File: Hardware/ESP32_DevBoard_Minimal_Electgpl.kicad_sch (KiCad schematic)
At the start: 36 parts, among them J1 U254-051T-4BH83-F1S, J2 Conn_01x22_Pin, J3 Conn_01x22_Pin, SW1 SW_Push, U1 MCP1826S-3302E/DB, U2 ESP32-S3, U3 W25Q64JVSSIQ, Y1 R940000096

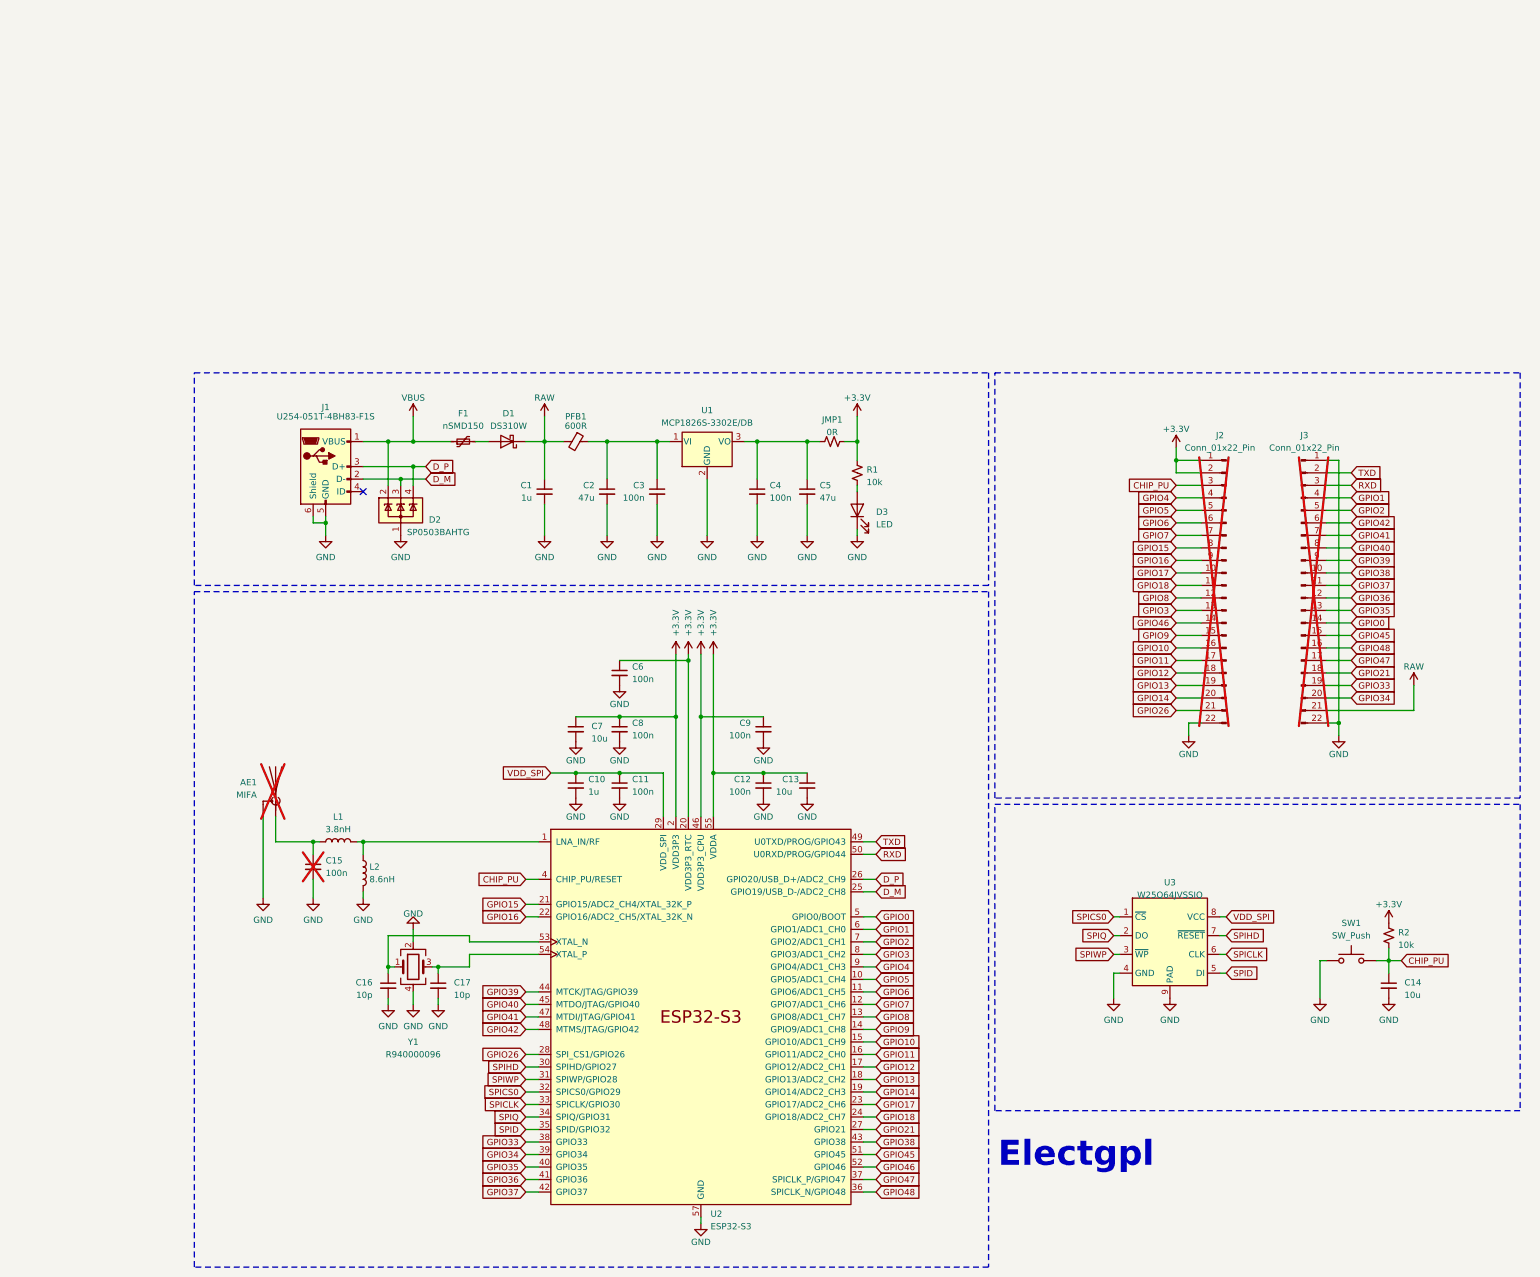
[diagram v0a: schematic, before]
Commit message: feather format and DRC check
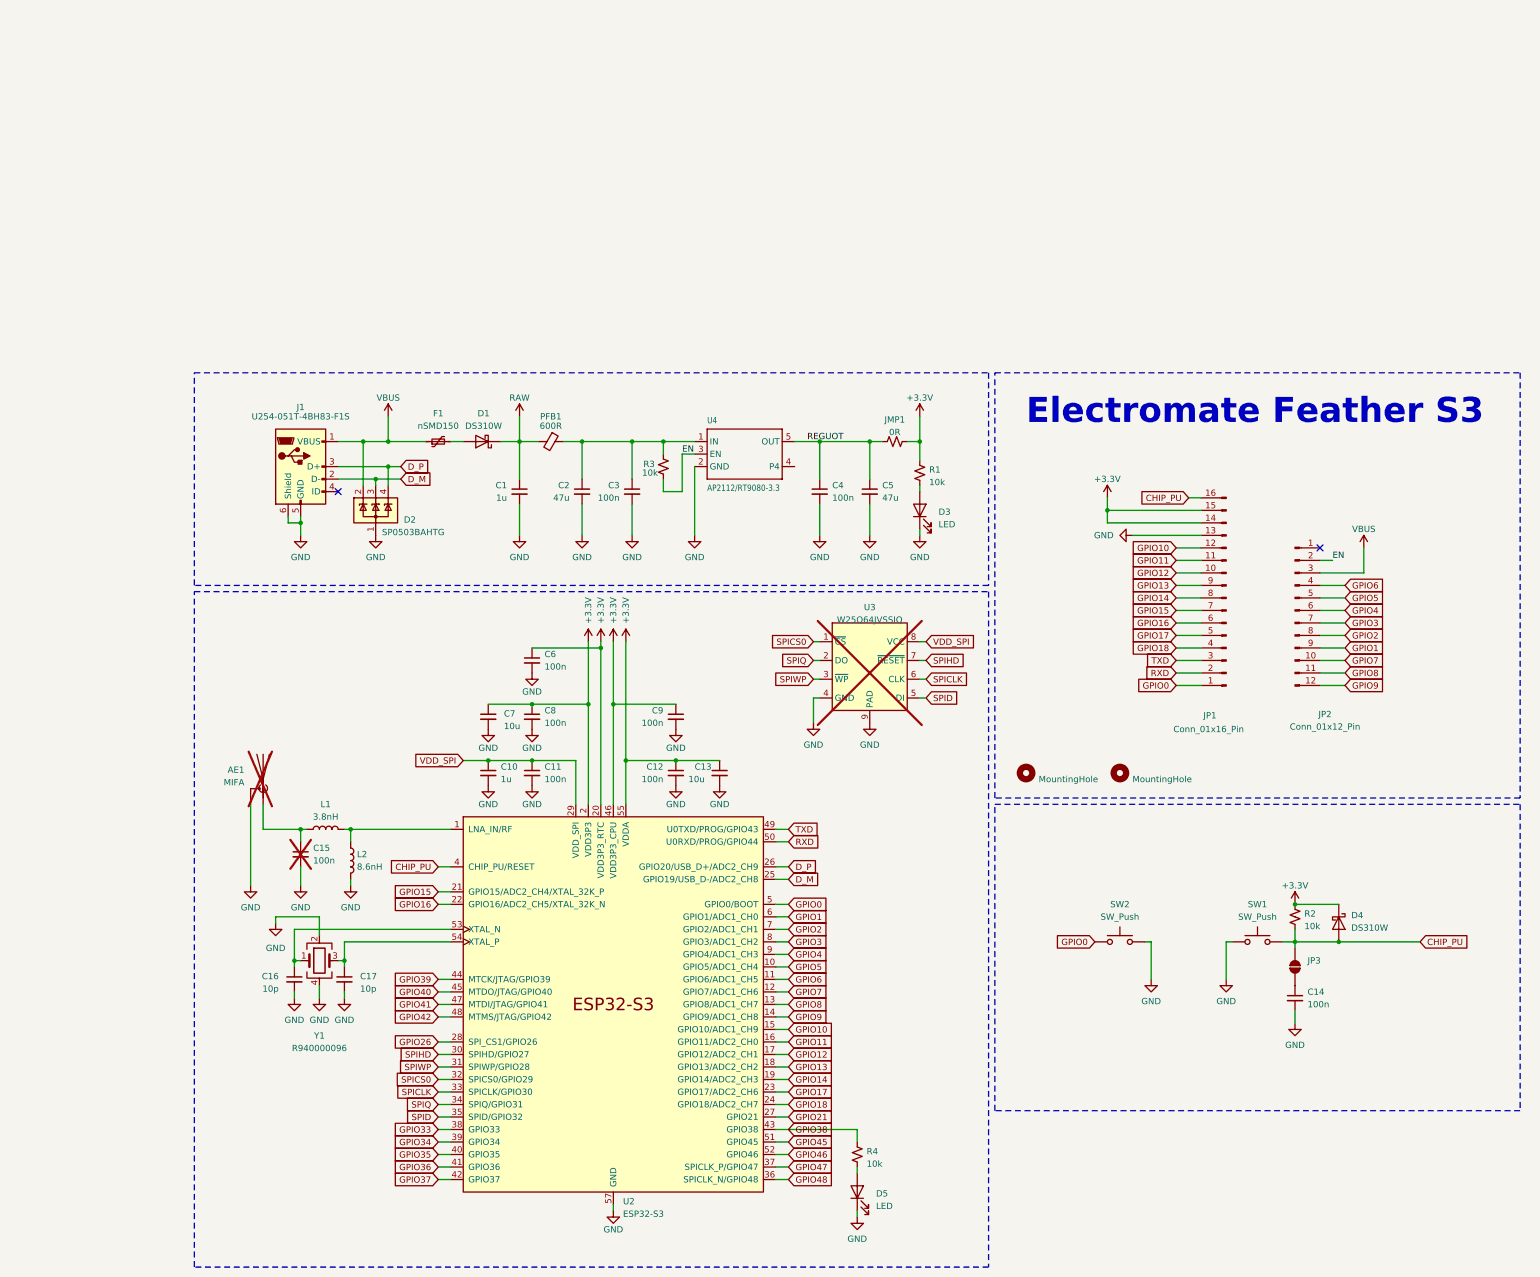
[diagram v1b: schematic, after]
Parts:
- removed U1: MCP1826S-3302E/DB, Package_TO_SOT_SMD:SOT-223, symbol Regulator_Linear:MCP1703Ax-330xxDB
- added D4: DS310W, Diode_SMD:D_SOD-123, symbol Diode:B140-E3
- added D5: LED, LED_SMD:LED_0603_1608Metric, symbol Device:LED
- added H1, H2: MountingHole, symbol Mechanical:MountingHole
- added JP3: SolderJumper_2_Open, Jumper:SolderJumper-2_P1.3mm_Open_RoundedPad1.0x1.5mm, symbol Jumper:SolderJumper_2_Open
- added R3, R4: 10k, Resistor_SMD:R_0402_1005Metric, symbol Device:R_Small_US
- added SW2: SW_Push, Button_Switch_SMD:SW_Push_SPST_NO_Alps_SKRK, symbol Switch:SW_Push
- added U4: AP2112/RT9080-3.3, Package_TO_SOT_SMD:SOT-23-5_HandSoldering, symbol Adafruit ESP32-S3 8MB No PSRAM-eagle-import:VREG_SOT23-5
- C1: LCSC Part Number (none) -> C5673; MFR P/N CL05X105KP5NNNC -> (none); MPN (none) -> CL05X105KP5NNNC; Reference MFG P/N C5673 -> (none)
- C14: value 10u -> 100n; footprint Capacitor_SMD:C_0603_1608Metric -> Capacitor_SMD:C_0402_1005Metric; Absolute minimum (none) -> 50V; LCSC CA0384128 -> RE0187778; MFR P/N GCM188D70J106ME36D -> CC0402KRX7R9BB104; Reference MFG P/N (none) -> C1591
- C2: LCSC Part Number (none) -> C124129; Reference MFG P/N C124129 -> (none)
- C3: LCSC Part Number (none) -> C1591; MFR P/N CC0402KRX7R9BB104 -> (none); MPN (none) -> CC0402KRX7R9BB104; Reference MFG P/N C1591 -> (none)
- JP1: renamed from J3; value Conn_01x22_Pin -> Conn_01x16_Pin; footprint Connector_PinHeader_2.54mm:PinHeader_1x22_P2.54mm_Vertical -> Connector_PinHeader_2.54mm:PinHeader_1x16_P2.54mm_Vertical; symbol Connector:Conn_01x22_Pin -> Connector:Conn_01x16_Pin; now fitted
- JP2: renamed from J2; value Conn_01x22_Pin -> Conn_01x12_Pin; footprint Connector_PinHeader_2.54mm:PinHeader_1x22_P2.54mm_Vertical -> Connector_PinHeader_2.54mm:PinHeader_1x12_P2.54mm_Vertical; symbol Connector:Conn_01x22_Pin -> Connector:Conn_01x12_Pin; now fitted
- U2: LCSC RF15788811 -> (none); LCSC Part Number (none) -> C3013940; MFR P/N ESP32-S3R8 -> (none); MPN (none) -> ESP32-S3FH4R2
- U3: now not fitted
- Y1: LCSC C7206306 -> (none); LCSC Part Number (none) -> C7206306
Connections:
- net +3.3V: now also JP1.14 (Pin_14), JP1.15 (Pin_15), D4.1 (K); no longer JP2.1 (Pin_1), JP2.2 (Pin_2)
- net CHIP_PU: now also JP1.16 (Pin_16), D4.2 (A), JP3.2 (B); no longer C14.1, JP2.3 (Pin_3)
- net GND: now also JP1.13 (Pin_13), D5.1 (K), SW2.1, U4.2 (GND); no longer JP1.1 (Pin_1), JP1.22 (Pin_22), JP2.22 (Pin_22)
- net GPIO0: now also JP1.1 (Pin_1), SW2.2; no longer JP1.14 (Pin_14)
- net GPIO1: now also JP2.9 (Pin_9); no longer JP1.4 (Pin_4)
- net GPIO10: now also JP1.12 (Pin_12); no longer JP2.16 (Pin_16)
- net GPIO11: now also JP1.11 (Pin_11); no longer JP2.17 (Pin_17)
- net GPIO12: now also JP1.10 (Pin_10); no longer JP2.18 (Pin_18)
- net GPIO13: now also JP1.9 (Pin_9); no longer JP2.19 (Pin_19)
- net GPIO14: now also JP1.8 (Pin_8); no longer JP2.20 (Pin_20)
- net GPIO15: now also JP1.7 (Pin_7); no longer JP2.8 (Pin_8)
- net GPIO16: now also JP1.6 (Pin_6); no longer JP2.9 (Pin_9)
- net GPIO17: now also JP1.5 (Pin_5); no longer JP2.10 (Pin_10)
- net GPIO18: now also JP1.4 (Pin_4); no longer JP2.11 (Pin_11)
- net GPIO2: now also JP2.8 (Pin_8); no longer JP1.5 (Pin_5)
- net GPIO21: no longer JP1.18 (Pin_18)
- net GPIO26: no longer JP2.21 (Pin_21)
- net GPIO3: now also JP2.7 (Pin_7); no longer JP2.13 (Pin_13)
- net GPIO33: no longer JP1.19 (Pin_19)
- net GPIO34: no longer JP1.20 (Pin_20)
- net GPIO35: no longer JP1.13 (Pin_13)
- net GPIO36: no longer JP1.12 (Pin_12)
- net GPIO37: no longer JP1.11 (Pin_11)
- net GPIO38: now also R4.1; no longer JP1.10 (Pin_10)
- net GPIO39: no longer JP1.9 (Pin_9)
- net GPIO4: now also JP2.6 (Pin_6); no longer JP2.4 (Pin_4)
- net GPIO40: no longer JP1.8 (Pin_8)
- net GPIO41: no longer JP1.7 (Pin_7)
- net GPIO42: no longer JP1.6 (Pin_6)
- net GPIO45: no longer JP1.15 (Pin_15)
- net GPIO46: no longer JP2.14 (Pin_14)
- net GPIO47: no longer JP1.17 (Pin_17)
- net GPIO48: no longer JP1.16 (Pin_16)
- net GPIO6: now also JP2.4 (Pin_4); no longer JP2.6 (Pin_6)
- net GPIO7: now also JP2.10 (Pin_10); no longer JP2.7 (Pin_7)
- net GPIO8: now also JP2.11 (Pin_11); no longer JP2.12 (Pin_12)
- net GPIO9: now also JP2.12 (Pin_12); no longer JP2.15 (Pin_15)
- net RAW: no longer JP1.21 (Pin_21)
- net RXD: now also JP1.2 (Pin_2); no longer JP1.3 (Pin_3)
- net TXD: now also JP1.3 (Pin_3); no longer JP1.2 (Pin_2)
- net VBUS: now also JP2.3 (Pin_3)
- net REGUOT: now reaches C4.1, C5.1, JMP1.1
- net REGUOT: now also U4.5 (OUT)
- net at C2.1, C3.1, PFB1.1: now also R3.1, U4.1 (IN)
- new net: D5.2 (A), R4.2
- new net: C14.1, JP3.1 (A)
- new net EN: JP2.2 (Pin_2), R3.2, U4.3 (EN)
- no-connect marks 1 -> 2
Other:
- note added: "Electromate Feather S3"
- note removed: "Electgpl"
- company: Electgpl -> Electromate
- moved on the sheet: AE1, C1, C10, C11, C12, C13, C15, C16, C17, C2, C3, C4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

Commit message: add u.FL antenna connector
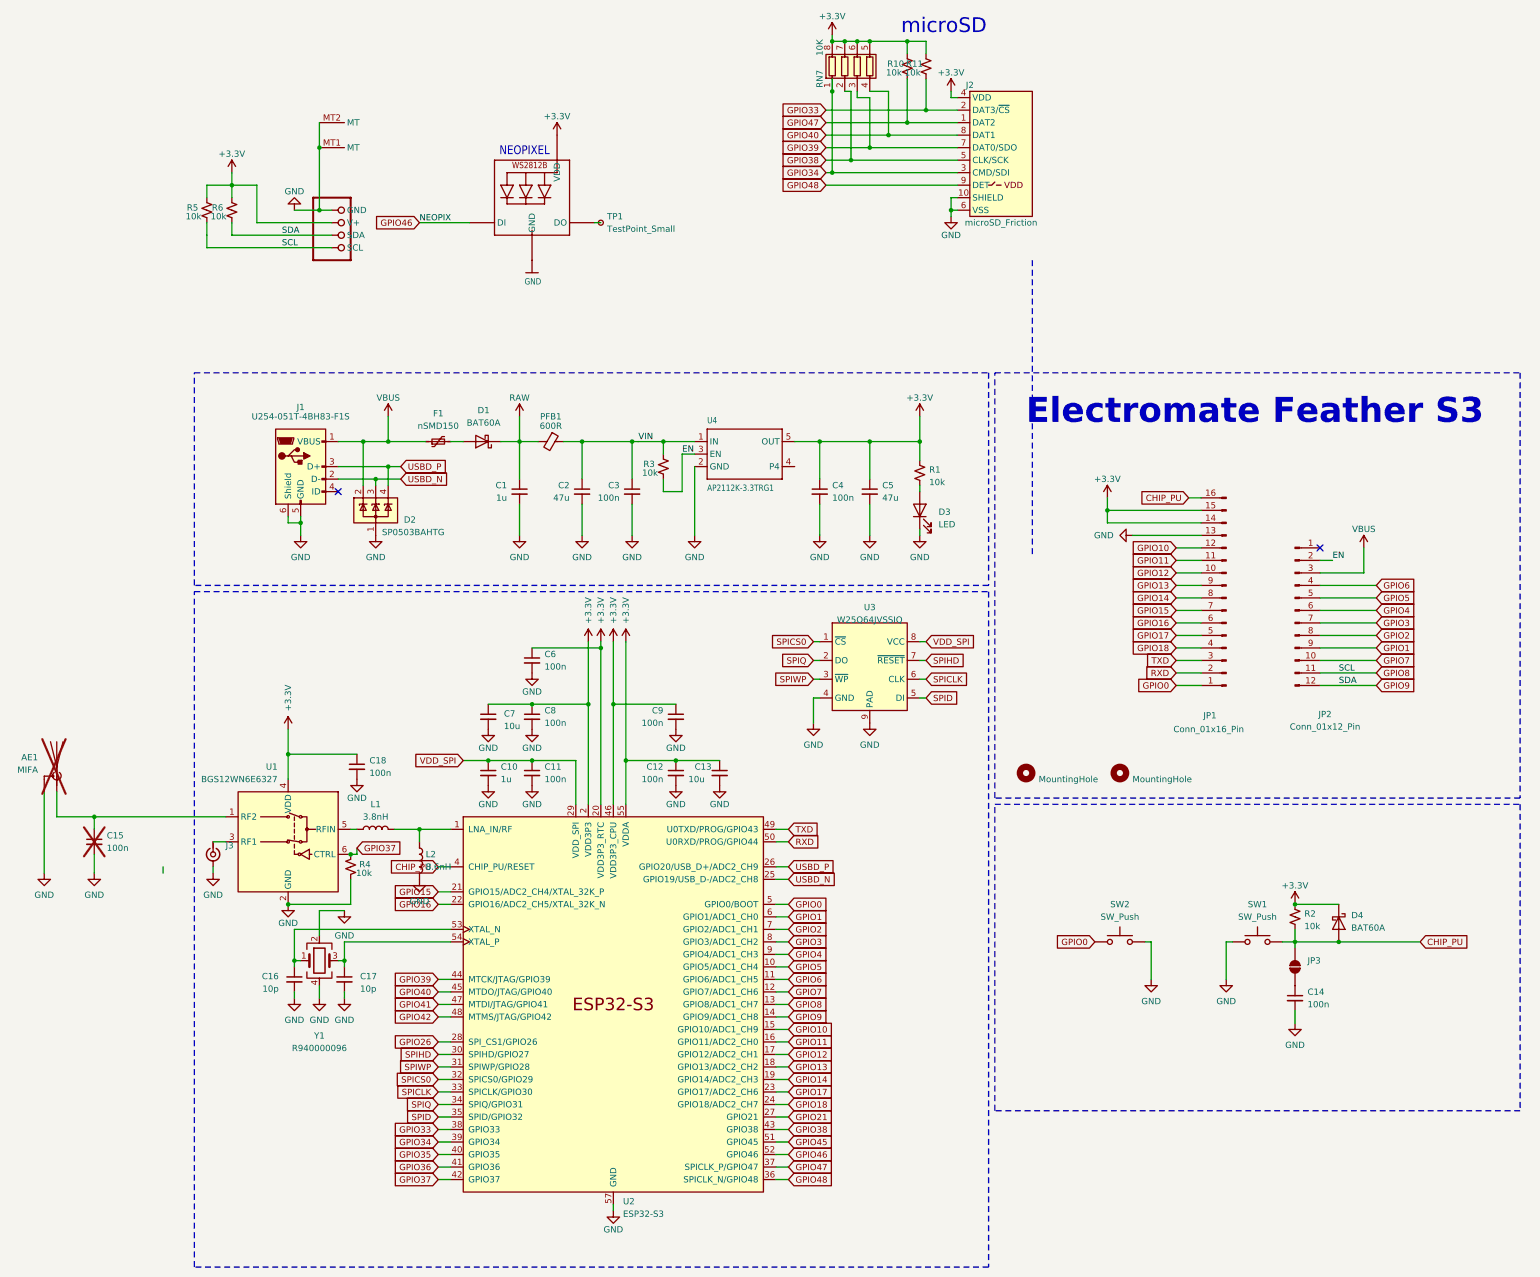
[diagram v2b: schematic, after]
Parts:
- removed D1, D4: DS310W, Diode_SMD:D_SOD-123, symbol Diode:B140-E3
- removed D5: LED, LED_SMD:LED_0603_1608Metric, symbol Device:LED
- removed JMP1: 0R, Resistor_SMD:R_0603_1608Metric, symbol Device:R_Small_US
- added C18: 100n, Capacitor_SMD:C_0402_1005Metric, symbol Device:C_Small
- added CONN1: QUICC, Connector_JST:JST_SH_BM04B-SRSS-TB_1x04-1MP_P1.00mm_Vertical, symbol Adafruit ESP32-S3 8MB No PSRAM-eagle-import:STEMMA_I2C_QTRA
- added D1, D4: BAT60A, Diode_SMD:D_SOD-323, symbol Diode:BAT60A
- added J2: microSD_Friction, Library:TF-SMD_TF-018, symbol SparkFun-Connector:microSD_Friction
- added J3: Conn_Coaxial_Small, Connector_Coaxial:U.FL_Molex_MCRF_73412-0110_Vertical, symbol Connector:Conn_Coaxial_Small
- added LED1: WS2812B_SK6805_1515, Library:LED-SMD_4P-L1.5-W1.5-BL, symbol Adafruit ESP32-S3 8MB No PSRAM-eagle-import:WS2812B_SK6805_1515
- added R10, R11, R5, R6: 10k, Resistor_SMD:R_0402_1005Metric, symbol Device:R_Small_US
- added RN7: 10K, Resistor_SMD:R_Array_Convex_4x0402, symbol Device:R_Pack04
- added TP1: TestPoint_Small, TestPoint:TestPoint_Pad_D1.0mm, symbol Connector:TestPoint_Small
- added U1: BGS12WN6E6327, Package_LGA:Infineon_PG-TSNP-6-10_0.7x1.1mm_0.7x1.1mm_P0.4mm, symbol RF_Switch:BGS12WN6E6327
- C10: MFR P/N CL05X105KP5NNNC -> (none); MPN (none) -> CL05X105KP5NNNC
- C11, C12, C14, C4, C6, C8, C9: MFR P/N CC0402KRX7R9BB104 -> (none); MPN (none) -> CC0402KRX7R9BB104
- C13, C7: MFR P/N GCM188D70J106ME36D -> (none); MPN (none) -> GCM188D70J106ME36D
- C16, C17: MFR P/N GRM1555C1H100GA01D -> (none); MPN (none) -> GRM1555C1H100GA01D
- C2, C5: MFR P/N GRM188R60J476ME15D -> (none); MPN (none) -> GRM188R60J476ME15D
- D2: MFR P/N SP0503BAHTG -> (none); MPN (none) -> SP0503BAHTG
- D3: MFR P/N TJ-S1608B06HQYJY-A3 -> (none); MPN (none) -> TJ-S1608B06HQYJY-A3
- F1: MFR P/N nSMD075-16V -> (none); MPN (none) -> nSMD075-16V
- J1: MFR P/N U254-051T-4BH83-F1S -> (none); MPN (none) -> U254-051T-4BH83-F1S
- L1: MFR P/N SCC1005C4N3SSP -> (none); MPN (none) -> SCC1005C4N3SSP
- L2: MFR P/N SCW1005C8N2JST -> (none); MPN (none) -> SCW1005C8N2JST
- PFB1: MFR P/N BLM18SG331TN1D -> (none); MPN (none) -> BLM18SG331TN1D
- R1, R2, R3, R4: MFR P/N RC0402JR-0710KL -> (none); MPN (none) -> RC0402JR-0710KL
- SW1, SW2: MFR P/N SKRKAEE020 -> (none); MPN (none) -> SKRKAEE020
- U3: MFR P/N GD25Q64ESIG -> (none); MPN (none) -> GD25Q64ESIG; now fitted
- U4: value AP2112/RT9080-3.3 -> AP2112K-3.3TRG1; footprint Package_TO_SOT_SMD:SOT-23-5_HandSoldering -> Package_TO_SOT_SMD:SOT-23-5; LCSC Part Number (none) -> C51118; MPN (none) -> AP2112K-3.3TRG1; Mfr (none) -> DIODES
- Y1: MFR P/N TAXM40M4ZHBCDT2T -> (none); MPN (none) -> TAXM40M4ZHBCDT2T
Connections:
- net REGUOT is gone; now on net +3.3V: C4.1, C5.1, U4.5 (OUT)
- net +3.3V: now also C18.1, CONN1.2 (V+), D4.1 (K), J2.4 (VDD), LED1.2 (VDD), R10.1, R11.1, R5.1, R6.1, RN7.5 (R4.2), RN7.6 (R3.2), RN7.7 (R2.2), RN7.8 (R1.2), U1.4 (VDD)
- net CHIP_PU: now also D4.2 (A)
- net GND: now also R4.2, C18.2, CONN1.1 (GND), CONN1.MT1 (MT), CONN1.MT2 (MT), J2.10 (SHIELD), J2.6 (VSS), J3.2 (Ext), LED1.4 (GND), U1.2 (GND)
- net GPIO33: now also J2.2 (DAT3/~{CS}), R11.2
- net GPIO34: now also J2.3 (CMD/SDI), RN7.1 (R1.1)
- net GPIO37: now also R4.1, U1.6 (CTRL)
- net GPIO38: now also J2.5 (CLK/SCK), RN7.2 (R2.1); no longer R4.1
- net GPIO39: now also J2.7 (DAT0/SDO), RN7.3 (R3.1)
- net GPIO40: now also J2.8 (DAT1), RN7.4 (R4.1)
- net GPIO46: now also LED1.1 (DI)
- net GPIO47: now also J2.1 (DAT2), R10.2
- net GPIO48: now also J2.9 (DET)
- net GPIO8: now also CONN1.4 (SCL), R5.2
- net GPIO9: now also CONN1.3 (SDA), R6.2
- net RAW: now also D1.1 (K)
- net at AE1.1 (A), C15.1: now also U1.1 (RF2); no longer L1.1
- net VIN: now reaches C2.1, C3.1, PFB1.1, R3.1, U4.1 (IN)
- net at F1.2: now also D1.2 (A)
- net D_M renamed USBD_N
- net D_P renamed USBD_P
- new net: LED1.3 (DO), TP1.1
- new net: L1.1, U1.5 (RFIN)
- new net: J3.1 (In), U1.3 (RF1)
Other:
- note added: "NEOPIXEL"
- note added: "microSD"
- moved on the sheet: AE1, C15, L1, L2
